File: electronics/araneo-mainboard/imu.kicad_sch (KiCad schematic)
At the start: 1 part, among them IC1 BMI270

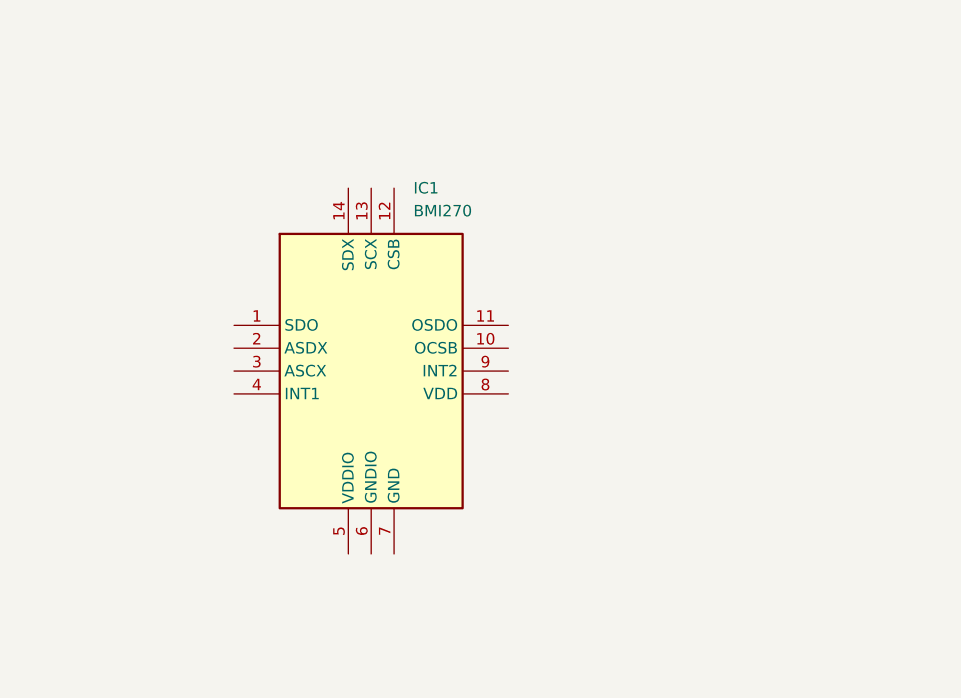
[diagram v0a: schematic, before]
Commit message: add components schematics
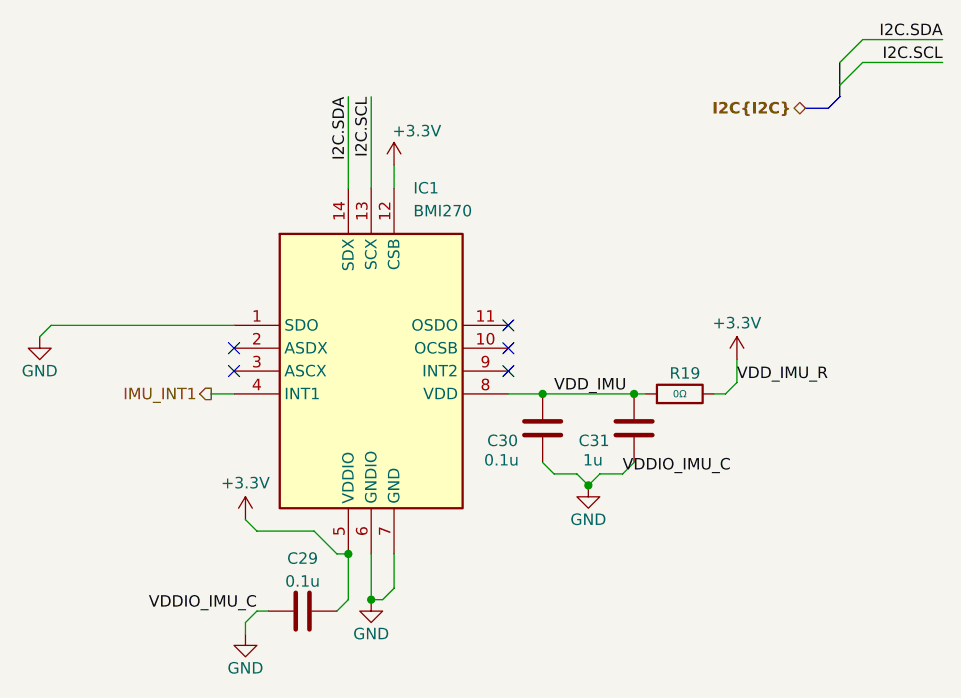
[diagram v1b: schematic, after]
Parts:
- added C29, C30: 0.1u, Diode_SMD:D_SMF, symbol Device:C
- added C31: 1u, Diode_SMD:D_SMF, symbol Device:C
- added R19: 0Ω, PCM_JLCPCB:R_0402, symbol PCM_JLCPCB-Resistors:0402,1.2kΩ
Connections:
- net GND: now reaches IC1.1 (SDO)
- net GND: now also IC1.6 (GNDIO), IC1.7 (GND), C29.1, C30.1, C31.1
- net +3.3V: now reaches IC1.12 (CSB)
- net +3.3V: now also IC1.5 (VDDIO), C29.2, R19.2
- net I2C.SCL: now reaches IC1.13 (SCX)
- net I2C.SDA: now reaches IC1.14 (SDX)
- net IMU_INT1: now reaches IC1.4 (INT1)
- net VDD_IMU: now reaches IC1.8 (VDD)
- net VDD_IMU: now also C30.2, C31.2, R19.1
- no-connect marks 0 -> 5

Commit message: electronics: assign footprints
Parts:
- C29, C30, C31: footprint Diode_SMD:D_SMF -> PCM_JLCPCB:C_0402
- IC1: footprint BMI270 -> Custom:BMI270
- R19: footprint PCM_JLCPCB:R_0402 -> PCM_JLCPCB:R_0603
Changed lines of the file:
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@@
 			)
 		)
-		(property "Footprint" "Diode_SMD:D_SMF"
+		(property "Footprint" "PCM_JLCPCB:C_0402"
 			(at 165.4048 93.98 0)
 			(hide yes)
@@
 			)
 		)
-		(property "Footprint" "PCM_JLCPCB:R_0402"
+		(property "Footprint" "PCM_JLCPCB:R_0603"
 			(at 171.45 95.758 90)
 			(hide yes)
@@
 			)
 		)
-		(property "Footprint" "BMI270"
+		(property "Footprint" "Custom:BMI270"
 			(at 148.59 173.66 0)
 			(hide yes)
@@
 			)
 		)
-		(property "Footprint" "Diode_SMD:D_SMF"
+		(property "Footprint" "PCM_JLCPCB:C_0402"
 			(at 133.35 117.1448 0)
 			(hide yes)
@@
 			)
 		)
-		(property "Footprint" "Diode_SMD:D_SMF"
+		(property "Footprint" "PCM_JLCPCB:C_0402"
 			(at 155.2448 93.98 0)
 			(hide yes)

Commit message: add missing components
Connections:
- net I2C.SCL renamed I2C1.SCL
- net I2C.SDA renamed I2C1.SDA
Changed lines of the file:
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@@
 		)
 	)
-	(label "I2C.SCL"
+	(label "I2C1.SCL"
 		(at 200.66 57.15 180)
 		(effects
@@
 		)
 	)
-	(label "I2C.SDA"
+	(label "I2C1.SDA"
 		(at 200.66 54.61 180)
 		(effects
@@
 		)
 	)
-	(label "I2C.SDA"
+	(label "I2C1.SDA"
 		(at 134.62 60.96 270)
 		(effects
@@
 		)
 	)
-	(label "I2C.SCL"
+	(label "I2C1.SCL"
 		(at 137.16 60.96 270)
 		(effects
@@
 		)
 	)
-	(hierarchical_label "I2C{I2C}"
+	(hierarchical_label "I2C1{I2C}"
 		(shape bidirectional)
 		(at 185.42 62.23 180)

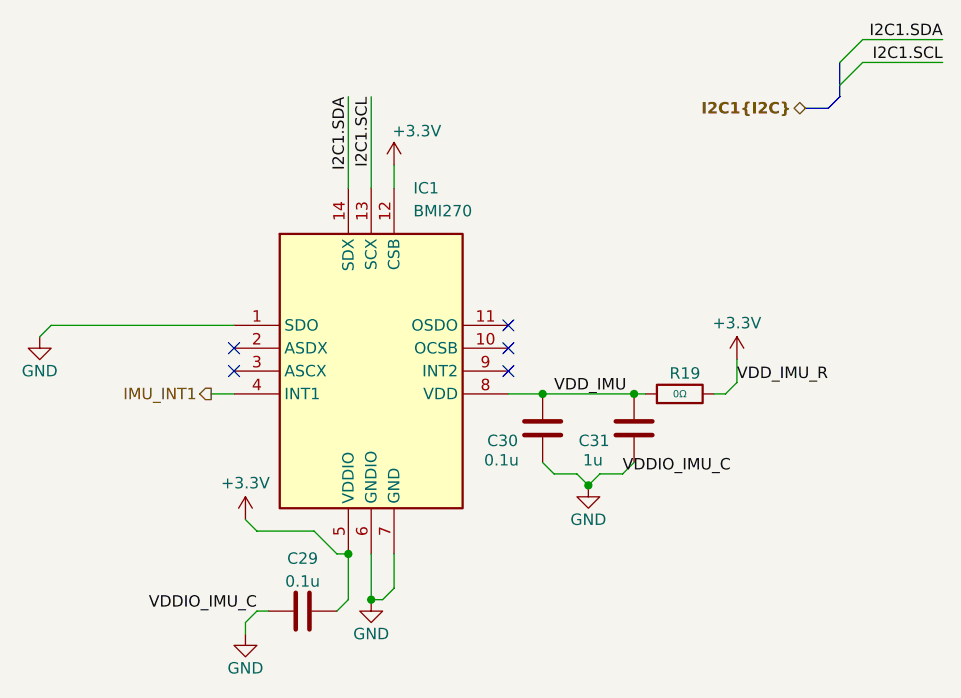
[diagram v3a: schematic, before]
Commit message: improve schematic and layout, add LCSC parts
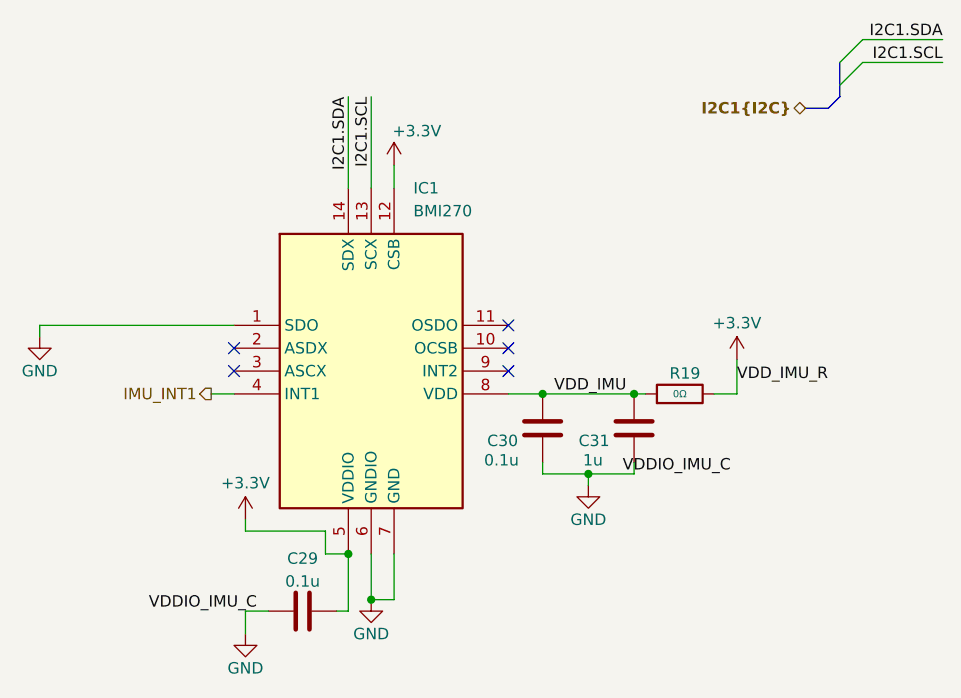
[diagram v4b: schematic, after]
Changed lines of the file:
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@@
 	(paper "A4")
 	(junction
-		(at 161.29 104.14)
-		(diameter 0)
-		(color 0 0 0 0)
-	)
-	(junction
 		(at 156.21 93.98)
+		(diameter 0)
+		(color 0 0 0 0)
+	)
+	(junction
+		(at 161.29 102.87)
 		(diameter 0)
 		(color 0 0 0 0)
@@
 	(wire
 		(pts
+			(xy 123.19 109.22) (xy 132.08 109.22)
+		)
+		(stroke
+			(width 0)
+			(type default)
+		)
+	)
+	(wire
+		(pts
 			(xy 139.7 68.58) (xy 139.7 71.12)
 		)
@@
 	(wire
 		(pts
-			(xy 162.56 102.87) (xy 161.29 104.14)
-		)
-		(stroke
-			(width 0)
-			(type default)
-		)
-	)
-	(wire
-		(pts
-			(xy 175.26 93.98) (xy 176.53 93.98)
-		)
-		(stroke
-			(width 0)
-			(type default)
-		)
-	)
-	(wire
-		(pts
-			(xy 100.33 87.63) (xy 101.6 86.36)
-		)
-		(stroke
-			(width 0)
-			(type default)
-		)
-	)
-	(wire
-		(pts
-			(xy 162.56 102.87) (xy 165.1 102.87)
-		)
-		(stroke
-			(width 0)
-			(type default)
-		)
-	)
-	(wire
-		(pts
-			(xy 137.16 116.84) (xy 138.43 116.84)
+			(xy 175.26 93.98) (xy 177.8 93.98)
+		)
+		(stroke
+			(width 0)
+			(type default)
+		)
+	)
+	(wire
+		(pts
+			(xy 137.16 116.84) (xy 139.7 116.84)
+		)
+		(stroke
+			(width 0)
+			(type default)
+		)
+	)
+	(wire
+		(pts
+			(xy 132.08 109.22) (xy 132.08 111.76)
 		)
 		(stroke
@@
 	(wire
 		(pts
-			(xy 124.46 118.11) (xy 125.73 118.11)
-		)
-		(stroke
-			(width 0)
-			(type default)
-		)
-	)
-	(wire
-		(pts
-			(xy 134.62 116.84) (xy 133.35 118.11)
-		)
-		(stroke
-			(width 0)
-			(type default)
-		)
-	)
-	(wire
-		(pts
-			(xy 123.19 119.38) (xy 123.19 120.65)
-		)
-		(stroke
-			(width 0)
-			(type default)
-		)
-	)
-	(wire
-		(pts
-			(xy 130.81 109.22) (xy 133.35 111.76)
-		)
-		(stroke
-			(width 0)
-			(type default)
-		)
-	)
-	(wire
-		(pts
-			(xy 134.62 111.76) (xy 134.62 116.84)
-		)
-		(stroke
-			(width 0)
-			(type default)
-		)
-	)
-	(wire
-		(pts
-			(xy 157.48 102.87) (xy 156.21 101.6)
-		)
-		(stroke
-			(width 0)
-			(type default)
-		)
-	)
-	(wire
-		(pts
-			(xy 124.46 109.22) (xy 130.81 109.22)
+			(xy 133.35 118.11) (xy 134.62 118.11)
+		)
+		(stroke
+			(width 0)
+			(type default)
+		)
+	)
+	(wire
+		(pts
+			(xy 156.21 101.6) (xy 156.21 102.87)
+		)
+		(stroke
+			(width 0)
+			(type default)
+		)
+	)
+	(wire
+		(pts
+			(xy 166.37 101.6) (xy 166.37 102.87)
+		)
+		(stroke
+			(width 0)
+			(type default)
+		)
+	)
+	(wire
+		(pts
+			(xy 134.62 111.76) (xy 134.62 118.11)
+		)
+		(stroke
+			(width 0)
+			(type default)
+		)
+	)
+	(wire
+		(pts
+			(xy 161.29 102.87) (xy 161.29 104.14)
 		)
 		(stroke
@@
 	(wire
 		(pts
-			(xy 123.19 107.95) (xy 124.46 109.22)
+			(xy 161.29 102.87) (xy 166.37 102.87)
+		)
+		(stroke
+			(width 0)
+			(type default)
+		)
+	)
+	(wire
+		(pts
+			(xy 132.08 111.76) (xy 134.62 111.76)
+		)
+		(stroke
+			(width 0)
+			(type default)
+		)
+	)
+	(wire
+		(pts
+			(xy 123.19 107.95) (xy 123.19 109.22)
+		)
+		(stroke
+			(width 0)
+			(type default)
+		)
+	)
+	(wire
+		(pts
+			(xy 156.21 102.87) (xy 161.29 102.87)
 		)
 		(stroke
@@
 	(wire
 		(pts
-			(xy 101.6 86.36) (xy 121.92 86.36)
-		)
-		(stroke
-			(width 0)
-			(type default)
-		)
-	)
-	(wire
-		(pts
 			(xy 137.16 60.96) (xy 137.16 71.12)
 		)
@@
 	(wire
 		(pts
+			(xy 123.19 118.11) (xy 123.19 120.65)
+		)
+		(stroke
+			(width 0)
+			(type default)
+		)
+	)
+	(wire
+		(pts
 			(xy 152.4 93.98) (xy 156.21 93.98)
 		)
@@
 	(wire
 		(pts
+			(xy 123.19 118.11) (xy 125.73 118.11)
+		)
+		(stroke
+			(width 0)
+			(type default)
+		)
+	)
+	(wire
+		(pts
 			(xy 119.38 93.98) (xy 121.92 93.98)
 		)
@@
 	(wire
 		(pts
-			(xy 157.48 102.87) (xy 160.02 102.87)
-		)
-		(stroke
-			(width 0)
-			(type default)
-		)
-	)
-	(wire
-		(pts
-			(xy 166.37 101.6) (xy 165.1 102.87)
-		)
-		(stroke
-			(width 0)
-			(type default)
-		)
-	)
-	(wire
-		(pts
-			(xy 177.8 90.17) (xy 177.8 92.71)
-		)
-		(stroke
-			(width 0)
-			(type default)
-		)
-	)
-	(wire
-		(pts
-			(xy 177.8 92.71) (xy 176.53 93.98)
-		)
-		(stroke
-			(width 0)
-			(type default)
-		)
-	)
-	(wire
-		(pts
-			(xy 139.7 115.57) (xy 138.43 116.84)
-		)
-		(stroke
-			(width 0)
-			(type default)
-		)
-	)
-	(wire
-		(pts
-			(xy 139.7 111.76) (xy 139.7 115.57)
-		)
-		(stroke
-			(width 0)
-			(type default)
-		)
-	)
-	(wire
-		(pts
-			(xy 161.29 104.14) (xy 160.02 102.87)
+			(xy 177.8 90.17) (xy 177.8 93.98)
+		)
+		(stroke
+			(width 0)
+			(type default)
+		)
+	)
+	(wire
+		(pts
+			(xy 139.7 111.76) (xy 139.7 116.84)
+		)
+		(stroke
+			(width 0)
+			(type default)
+		)
+	)
+	(wire
+		(pts
+			(xy 100.33 86.36) (xy 121.92 86.36)
 		)
 		(stroke
@@
 	(wire
 		(pts
-			(xy 133.35 111.76) (xy 134.62 111.76)
+			(xy 100.33 86.36) (xy 100.33 87.63)
 		)
 		(stroke
@@
 		)
 		(stroke
-			(width 0)
-			(type default)
-		)
-	)
-	(wire
-		(pts
-			(xy 123.19 119.38) (xy 124.46 118.11)
-		)
-		(stroke
